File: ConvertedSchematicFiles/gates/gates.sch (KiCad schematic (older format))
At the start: 15 parts, among them U1 7408, U2 7432, U3 7400, U4 7402, U5 7486

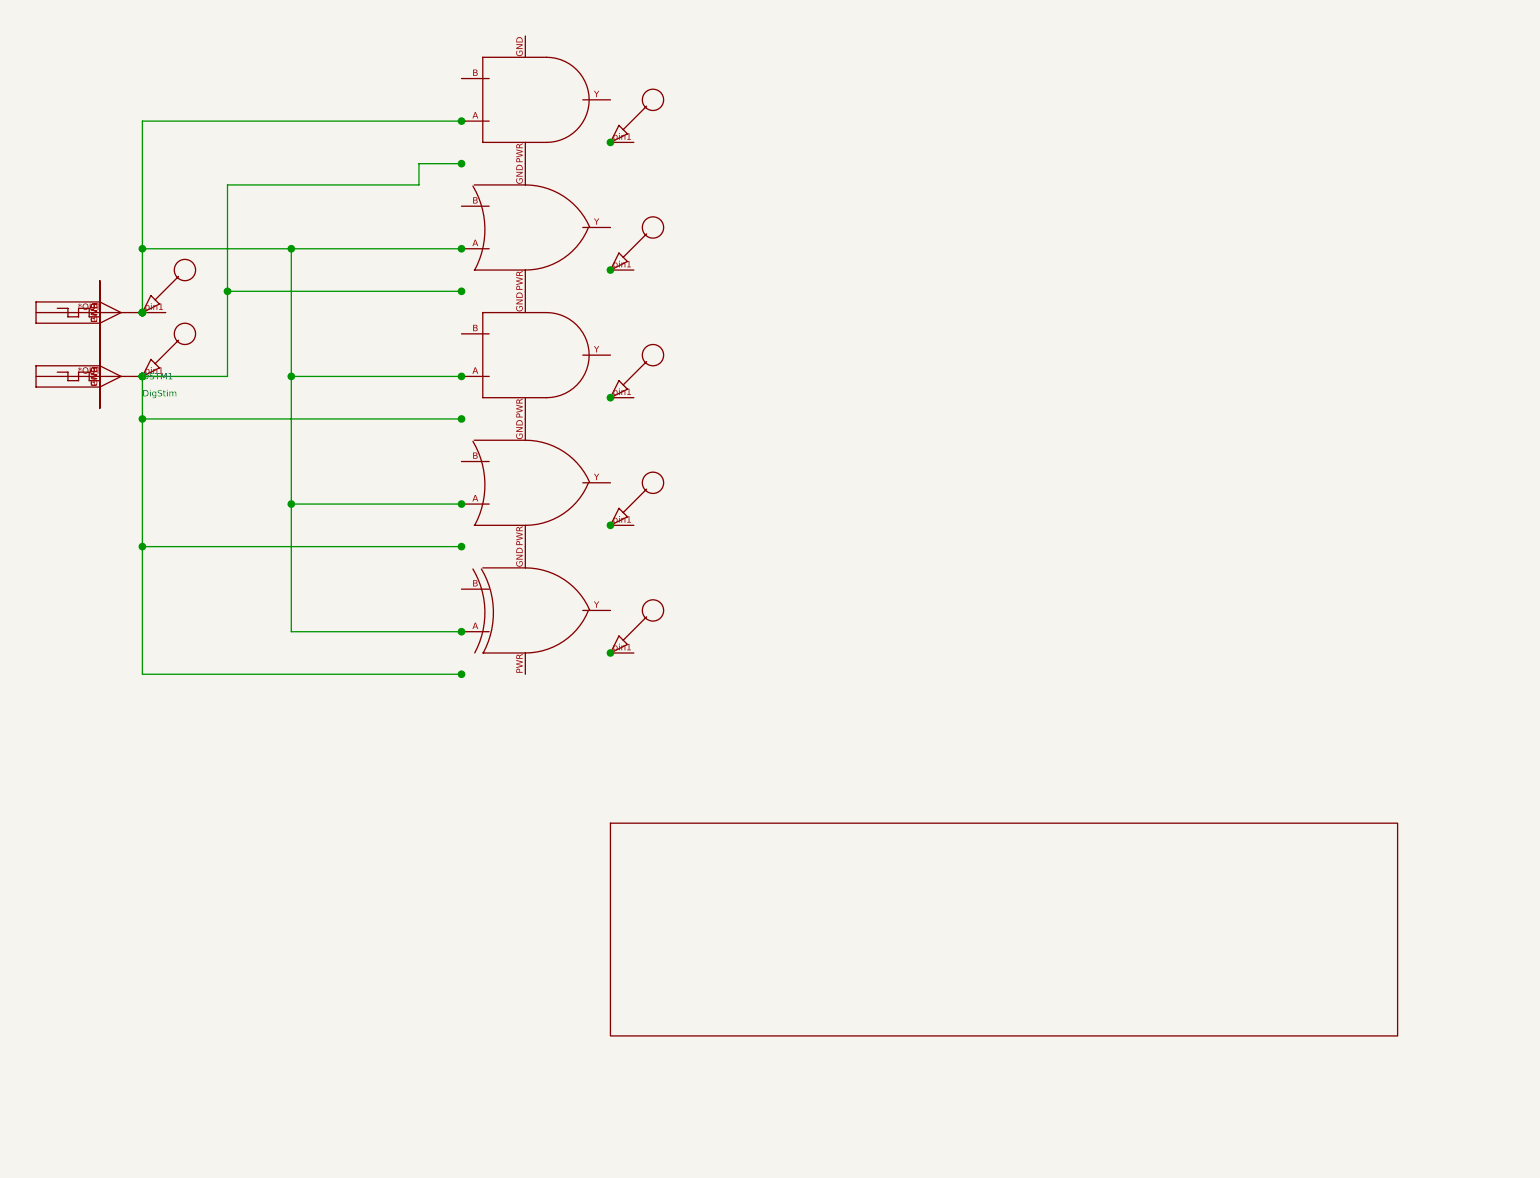
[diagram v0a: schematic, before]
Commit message: Excluded some components. These no longer appear after conversion. When calling shell commands, filenames are in "quotes"
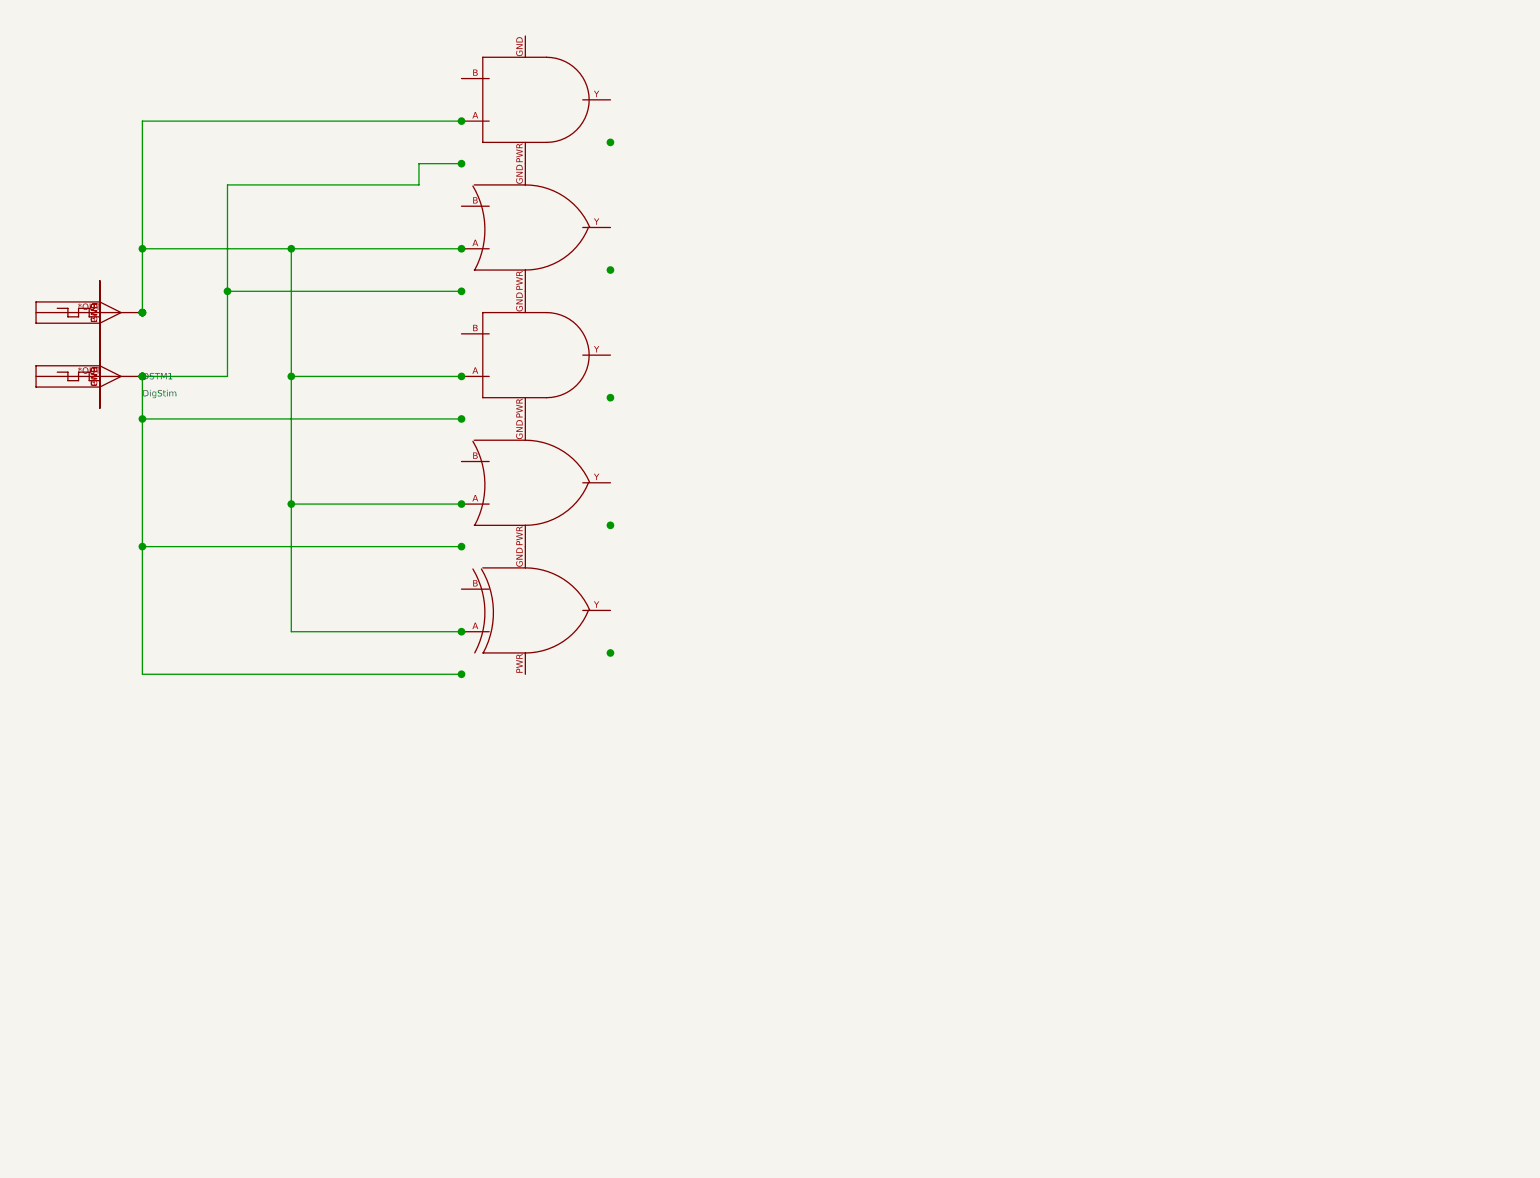
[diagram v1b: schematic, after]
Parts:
- removed nodeMarker (x7): nodeMarker, symbol NODEMARKER_PSPICE
- removed titleblk: titleblk, symbol TITLEBLK_PSPICE
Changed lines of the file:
@@
-	1    0    0    1
-$EndComp
-$Comp
-L TITLEBLK_PSPICE titleblk
-U 1 1 39760492
-P 9700 7200
-F 0 "titleblk" H 19400 14400 30  0001 L CNN
-F 1 "titleblk" H 19400 14480 30  0001 L CNN
-	1    9700 7200
-	1    0    0    1
-$EndComp
-$Comp
-L NODEMARKER_PSPICE nodeMarker
-U 1 1 66516649
-P 6000 3000
-F 0 "nodeMarker" H 12000 6000 30  0001 L CNN
-F 1 "nodeMarker" H 12000 6080 30  0001 L CNN
-	1    6000 3000
-	1    0    0    1
-$EndComp
-$Comp
-L NODEMARKER_PSPICE nodeMarker
-U 1 1 29641421
-P 6000 3600
-F 0 "nodeMarker" H 12000 7200 30  0001 L CNN
-F 1 "nodeMarker" H 12000 7280 30  0001 L CNN
-	1    6000 3600
-	1    0    0    1
-$EndComp
-$Comp
-L NODEMARKER_PSPICE nodeMarker
-U 1 1 45202362
-P 6000 4200
-F 0 "nodeMarker" H 12000 8400 30  0001 L CNN
-F 1 "nodeMarker" H 12000 8480 30  0001 L CNN
-	1    6000 4200
-	1    0    0    1
-$EndComp
-$Comp
-L NODEMARKER_PSPICE nodeMarker
-U 1 1 10490027
-P 6000 4800
-F 0 "nodeMarker" H 12000 9600 30  0001 L CNN
-F 1 "nodeMarker" H 12000 9680 30  0001 L CNN
-	1    6000 4800
-	1    0    0    1
-$EndComp
-$Comp
-L NODEMARKER_PSPICE nodeMarker
-U 1 1 73368690
-P 6000 5400
-F 0 "nodeMarker" H 12000 10800 30  0001 L CNN
-F 1 "nodeMarker" H 12000 10880 30  0001 L CNN
-	1    6000 5400
-	1    0    0    1
-$EndComp
-$Comp
-L NODEMARKER_PSPICE nodeMarker
-U 1 1 32520059
-P 3800 3800
-F 0 "nodeMarker" H 7600 7600 30  0001 L CNN
-F 1 "nodeMarker" H 7600 7680 30  0001 L CNN
-	1    3800 3800
-	1    0    0    1
-$EndComp
-$Comp
-L NODEMARKER_PSPICE nodeMarker
-U 1 1 74897763
-P 3800 4100
-F 0 "nodeMarker" H 7600 8200 30  0001 L CNN
-F 1 "nodeMarker" H 7600 8280 30  0001 L CNN
-	1    3800 4100
 	1    0    0    1
 $EndComp

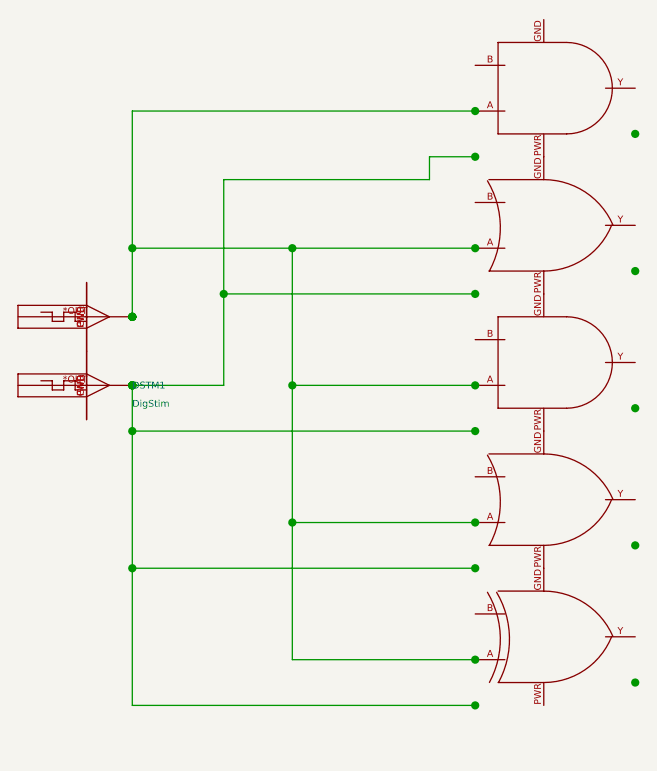
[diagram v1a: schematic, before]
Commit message: Orientation fix. Library components are now inverted, with +ve y axis going up. In Schematic files, +ve y axis is downwards. This is how the KiCad libraries are. As a result of the above fixed, the converted GND is now oriented correctly.
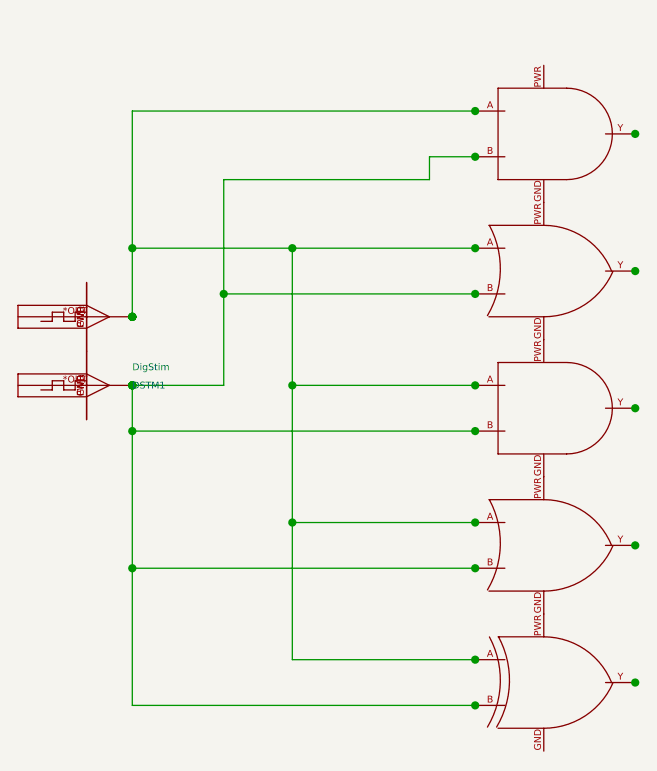
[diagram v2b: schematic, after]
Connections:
- net at U1.B: now also DSTM1.*OUT, U2.B, U3.B, U4.B, U5.B
- net at U1.GND: now also U2.PWR
- net at U1.PWR: no longer U2.GND
- net at U4.GND: now also U5.PWR; no longer U3.PWR
- net at U4.PWR: now also U3.GND; no longer U5.GND
- net at DSTM2.GND: now also DSTM1.PWR
- net at DSTM2.PWR: no longer DSTM1.GND
- new net: U2.GND, U3.PWR
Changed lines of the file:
@@
 F 1 "7408" H 5300 2980 30  0001 L CNN
 	1    5300 2900
-	1    0    0    1
+	1    0    0    -1
 $EndComp
 $Comp
@@
 F 1 "7432" H 5300 3580 30  0001 L CNN
 	1    5300 3500
-	1    0    0    1
+	1    0    0    -1
 $EndComp
 $Comp
@@
 F 1 "7400" H 5300 4180 30  0001 L CNN
 	1    5300 4100
-	1    0    0    1
+	1    0    0    -1
 $EndComp
 $Comp
@@
 F 1 "7402" H 5300 4780 30  0001 L CNN
 	1    5300 4700
-	1    0    0    1
+	1    0    0    -1
 $EndComp
 $Comp
@@
 F 1 "7486" H 5300 5380 30  0001 L CNN
 	1    5300 5300
-	1    0    0    1
+	1    0    0    -1
 $EndComp
 $Comp
@@
 F 1 "DigStim" H 3800 3880 30  0001 L CNN
 	1    3800 3800
-	1    0    0    1
+	1    0    0    -1
 $EndComp
 $Comp
@@
 F 1 "DigStim" H 3800 4180 30  0000 L CNN
 	1    3800 4100
-	1    0    0    1
+	1    0    0    -1
 $EndComp
 Wire Wire Line

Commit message: Removed the use of exec, wrote basename function, made integration with eSim easier.
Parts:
- added nodeMarker (x7): nodeMarker, symbol nodeMarker_PSPICE
- added titleblk: titleblk, symbol titleblk_PSPICE
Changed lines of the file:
@@
-EESchema Schematic File Version 2  date Sunday 27 June 1999 12:53:35 AM IST
+EESchema Schematic File Version 2  date
 LIBS:power
 LIBS:device
@@
 LIBS:contrib
 LIBS:valves
-LIBS:ConvertedSchematicFiles/gates-cache
 EELAYER 25  0
 EELAYER END
@@
 Sheet 1 1
 Title ""
-Date "27 Jun 1999"
+Date ""
 Rev ""
 Comp ""
@@
 	1    3800 4100
 	1    0    0    -1
+$EndComp
+$Comp
+L titleblk_PSPICE titleblk
+U 1 1 39760492
+P 9700 7200
+F 0 "titleblk" H 19400 14400 30  0001 L CNN
+F 1 "titleblk" H 19400 14480 30  0001 L CNN
+	1    9700 7200
+	1    0    0    -1
+$EndComp
+$Comp
+L nodeMarker_PSPICE nodeMarker
+U 1 1 66516649
+P 6000 3000
+F 0 "nodeMarker" H 12000 6000 30  0001 L CNN
+F 1 "nodeMarker" H 12000 6080 30  0001 L CNN
+	1    6000 3000
+	1    0    0    -1
+$EndComp
+$Comp
+L nodeMarker_PSPICE nodeMarker
+U 1 1 29641421
+P 6000 3600
+F 0 "nodeMarker" H 12000 7200 30  0001 L CNN
+F 1 "nodeMarker" H 12000 7280 30  0001 L CNN
+	1    6000 3600
+	1    0    0    -1
+$EndComp
+$Comp
+L nodeMarker_PSPICE nodeMarker
+U 1 1 45202362
+P 6000 4200
+F 0 "nodeMarker" H 12000 8400 30  0001 L CNN
+F 1 "nodeMarker" H 12000 8480 30  0001 L CNN
+	1    6000 4200
+	1    0    0    -1
+$EndComp
+$Comp
+L nodeMarker_PSPICE nodeMarker
+U 1 1 10490027
+P 6000 4800
+F 0 "nodeMarker" H 12000 9600 30  0001 L CNN
+F 1 "nodeMarker" H 12000 9680 30  0001 L CNN
+	1    6000 4800
+	1    0    0    -1
+$EndComp
+$Comp
+L nodeMarker_PSPICE nodeMarker
+U 1 1 73368690
+P 6000 5400
+F 0 "nodeMarker" H 12000 10800 30  0001 L CNN
+F 1 "nodeMarker" H 12000 10880 30  0001 L CNN
+	1    6000 5400
+	1    0    0    -1
+$EndComp
+$Comp
+L nodeMarker_PSPICE nodeMarker
+U 1 1 32520059
+P 3800 3800
+F 0 "nodeMarker" H 7600 7600 30  0001 L CNN
+F 1 "nodeMarker" H 7600 7680 30  0001 L CNN
+	1    3800 3800
+	1    0    0    -1
+$EndComp
+$Comp
+L nodeMarker_PSPICE nodeMarker
+U 1 1 74897763
+P 3800 4100
+F 0 "nodeMarker" H 7600 8200 30  0001 L CNN
+F 1 "nodeMarker" H 7600 8280 30  0001 L CNN
+	1    3800 4100
+	1    0    0    -1
